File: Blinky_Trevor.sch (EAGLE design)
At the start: 15 parts, among them IC1 OP-DUALRM

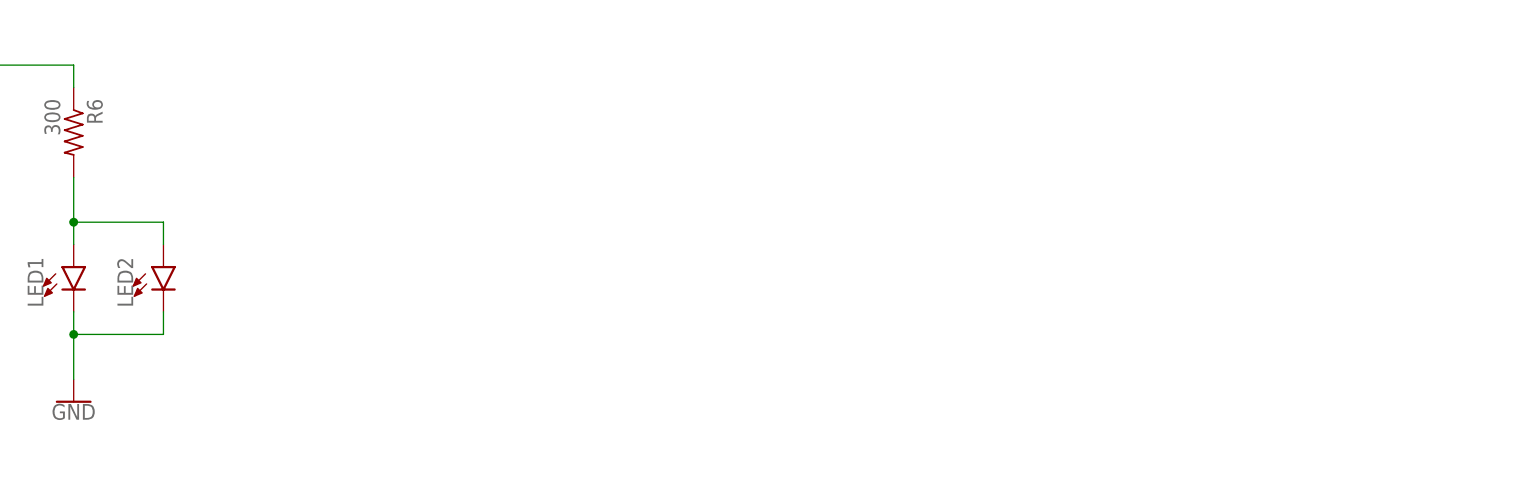
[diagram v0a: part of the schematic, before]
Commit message: Added LED Pattern
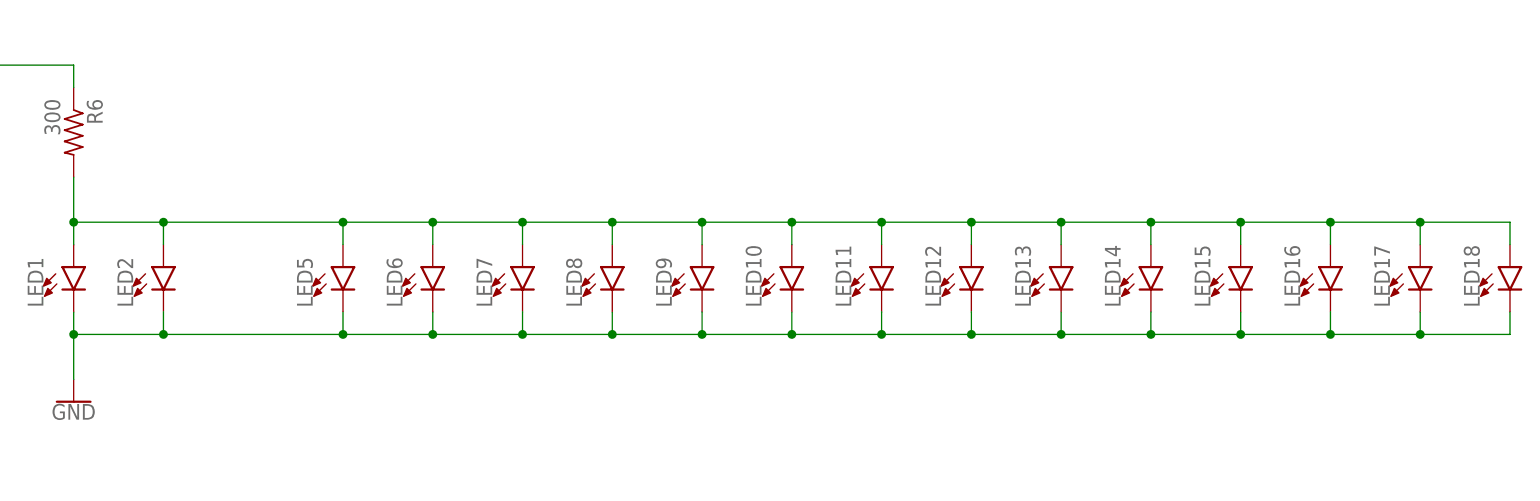
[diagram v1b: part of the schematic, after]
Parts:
- added LED10, LED11, LED12, LED13, LED14, LED15, LED16, LED17, LED18, LED5, LED6, LED7, LED8, LED9: (no value), CalvEngIO-LED:LED0603
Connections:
- net GND: now also LED10.C, LED11.C, LED12.C, LED13.C, LED14.C, LED15.C, LED16.C, LED17.C, LED18.C, LED5.C, LED6.C, LED7.C, LED8.C, LED9.C
- net N$6: now also LED10.A, LED11.A, LED12.A, LED13.A, LED14.A, LED15.A, LED16.A, LED17.A, LED18.A, LED5.A, LED6.A, LED7.A, LED8.A, LED9.A
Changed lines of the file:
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@@
 <part name="GND6" library="CalvEngIO-Symbols" deviceset="GND" device=""/>
 <part name="C2" library="CalvEngIO-Passives" deviceset="CAPACITOR" device="0402" value="100nF"/>
+<part name="LED5" library="CalvEngIO-LED" deviceset="LED" device="0603"/>
+<part name="LED6" library="CalvEngIO-LED" deviceset="LED" device="0603"/>
+<part name="LED7" library="CalvEngIO-LED" deviceset="LED" device="0603"/>
+<part name="LED8" library="CalvEngIO-LED" deviceset="LED" device="0603"/>
+<part name="LED9" library="CalvEngIO-LED" deviceset="LED" device="0603"/>
+<part name="LED10" library="CalvEngIO-LED" deviceset="LED" device="0603"/>
+<part name="LED11" library="CalvEngIO-LED" deviceset="LED" device="0603"/>
+<part name="LED12" library="CalvEngIO-LED" deviceset="LED" device="0603"/>
+<part name="LED13" library="CalvEngIO-LED" deviceset="LED" device="0603"/>
+<part name="LED14" library="CalvEngIO-LED" deviceset="LED" device="0603"/>
+<part name="LED15" library="CalvEngIO-LED" deviceset="LED" device="0603"/>
+<part name="LED16" library="CalvEngIO-LED" deviceset="LED" device="0603"/>
+<part name="LED17" library="CalvEngIO-LED" deviceset="LED" device="0603"/>
+<part name="LED18" library="CalvEngIO-LED" deviceset="LED" device="0603"/>
 </parts>
 <sheets>
@@
 <attribute name="VALUE" x="18.161" y="2.032" size="1.778" layer="96"/>
 </instance>
+<instance part="LED5" gate="G$1" x="187.96" y="25.4"/>
+<instance part="LED6" gate="G$1" x="198.12" y="25.4"/>
+<instance part="LED7" gate="G$1" x="208.28" y="25.4"/>
+<instance part="LED8" gate="G$1" x="218.44" y="25.4"/>
+<instance part="LED9" gate="G$1" x="228.6" y="25.4"/>
+<instance part="LED10" gate="G$1" x="238.76" y="25.4"/>
+<instance part="LED11" gate="G$1" x="248.92" y="25.4"/>
+<instance part="LED12" gate="G$1" x="259.08" y="25.4"/>
+<instance part="LED13" gate="G$1" x="269.24" y="25.4"/>
+<instance part="LED14" gate="G$1" x="279.4" y="25.4"/>
+<instance part="LED15" gate="G$1" x="289.56" y="25.4"/>
+<instance part="LED16" gate="G$1" x="299.72" y="25.4"/>
+<instance part="LED17" gate="G$1" x="309.88" y="25.4"/>
+<instance part="LED18" gate="G$1" x="320.04" y="25.4"/>
 </instances>
 <busses>
@@
 <wire x1="167.64" y1="17.78" x2="157.48" y2="17.78" width="0.1524" layer="91"/>
 <junction x="157.48" y="17.78"/>
+<pinref part="LED16" gate="G$1" pin="C"/>
+<wire x1="167.64" y1="17.78" x2="187.96" y2="17.78" width="0.1524" layer="91"/>
+<wire x1="187.96" y1="17.78" x2="198.12" y2="17.78" width="0.1524" layer="91"/>
+<wire x1="198.12" y1="17.78" x2="208.28" y2="17.78" width="0.1524" layer="91"/>
+<wire x1="208.28" y1="17.78" x2="218.44" y2="17.78" width="0.1524" layer="91"/>
+<wire x1="218.44" y1="17.78" x2="228.6" y2="17.78" width="0.1524" layer="91"/>
+<wire x1="228.6" y1="17.78" x2="238.76" y2="17.78" width="0.1524" layer="91"/>
+<wire x1="238.76" y1="17.78" x2="248.92" y2="17.78" width="0.1524" layer="91"/>
+<wire x1="248.92" y1="17.78" x2="259.08" y2="17.78" width="0.1524" layer="91"/>
+<wire x1="259.08" y1="17.78" x2="269.24" y2="17.78" width="0.1524" layer="91"/>
+<wire x1="269.24" y1="17.78" x2="279.4" y2="17.78" width="0.1524" layer="91"/>
+<wire x1="279.4" y1="17.78" x2="289.56" y2="17.78" width="0.1524" layer="91"/>
+<wire x1="289.56" y1="17.78" x2="299.72" y2="17.78" width="0.1524" layer="91"/>
+<wire x1="299.72" y1="17.78" x2="299.72" y2="20.32" width="0.1524" layer="91"/>
+<junction x="167.64" y="17.78"/>
+<pinref part="LED5" gate="G$1" pin="C"/>
+<wire x1="187.96" y1="20.32" x2="187.96" y2="17.78" width="0.1524" layer="91"/>
+<junction x="187.96" y="17.78"/>
+<pinref part="LED6" gate="G$1" pin="C"/>
+<wire x1="198.12" y1="20.32" x2="198.12" y2="17.78" width="0.1524" layer="91"/>
+<junction x="198.12" y="17.78"/>
+<pinref part="LED7" gate="G$1" pin="C"/>
+<wire x1="208.28" y1="20.32" x2="208.28" y2="17.78" width="0.1524" layer="91"/>
+<junction x="208.28" y="17.78"/>
+<pinref part="LED8" gate="G$1" pin="C"/>
+<wire x1="218.44" y1="20.32" x2="218.44" y2="17.78" width="0.1524" layer="91"/>
+<junction x="218.44" y="17.78"/>
+<pinref part="LED9" gate="G$1" pin="C"/>
+<wire x1="228.6" y1="20.32" x2="228.6" y2="17.78" width="0.1524" layer="91"/>
+<junction x="228.6" y="17.78"/>
+<pinref part="LED10" gate="G$1" pin="C"/>
+<wire x1="238.76" y1="20.32" x2="238.76" y2="17.78" width="0.1524" layer="91"/>
+<junction x="238.76" y="17.78"/>
+<pinref part="LED11" gate="G$1" pin="C"/>
+<wire x1="248.92" y1="20.32" x2="248.92" y2="17.78" width="0.1524" layer="91"/>
+<junction x="248.92" y="17.78"/>
+<pinref part="LED12" gate="G$1" pin="C"/>
+<wire x1="259.08" y1="20.32" x2="259.08" y2="17.78" width="0.1524" layer="91"/>
+<junction x="259.08" y="17.78"/>
+<pinref part="LED13" gate="G$1" pin="C"/>
+<wire x1="269.24" y1="20.32" x2="269.24" y2="17.78" width="0.1524" layer="91"/>
+<junction x="269.24" y="17.78"/>
+<pinref part="LED14" gate="G$1" pin="C"/>
+<wire x1="279.4" y1="20.32" x2="279.4" y2="17.78" width="0.1524" layer="91"/>
+<junction x="279.4" y="17.78"/>
+<pinref part="LED15" gate="G$1" pin="C"/>
+<wire x1="289.56" y1="20.32" x2="289.56" y2="17.78" width="0.1524" layer="91"/>
+<junction x="289.56" y="17.78"/>
+<pinref part="LED18" gate="G$1" pin="C"/>
+<wire x1="320.04" y1="20.32" x2="320.04" y2="17.78" width="0.1524" layer="91"/>
+<wire x1="320.04" y1="17.78" x2="309.88" y2="17.78" width="0.1524" layer="91"/>
+<junction x="299.72" y="17.78"/>
+<pinref part="LED17" gate="G$1" pin="C"/>
+<wire x1="309.88" y1="17.78" x2="299.72" y2="17.78" width="0.1524" layer="91"/>
+<wire x1="309.88" y1="20.32" x2="309.88" y2="17.78" width="0.1524" layer="91"/>
+<junction x="309.88" y="17.78"/>
 </segment>
 <segment>
@@
 <wire x1="167.64" y1="30.48" x2="167.64" y2="27.94" width="0.1524" layer="91"/>
 <junction x="157.48" y="30.48"/>
-</segment>
-</net>
+<pinref part="LED16" gate="G$1" pin="A"/>
+<wire x1="167.64" y1="30.48" x2="187.96" y2="30.48" width="0.1524" layer="91"/>
+<wire x1="187.96" y1="30.48" x2="198.12" y2="30.48" width="0.1524" layer="91"/>
+<wire x1="198.12" y1="30.48" x2="208.28" y2="30.48" width="0.1524" layer="91"/>
+<wire x1="208.28" y1="30.48" x2="218.44" y2="30.48" width="0.1524" layer="91"/>
+<wire x1="218.44" y1="30.48" x2="228.6" y2="30.48" width="0.1524" layer="91"/>
+<wire x1="228.6" y1="30.48" x2="238.76" y2="30.48" width="0.1524" layer="91"/>
+<wire x1="238.76" y1="30.48" x2="248.92" y2="30.48" width="0.1524" layer="91"/>
+<wire x1="248.92" y1="30.48" x2="259.08" y2="30.48" width="0.1524" layer="91"/>
+<wire x1="259.08" y1="30.48" x2="269.24" y2="30.48" width="0.1524" layer="91"/>
+<wire x1="269.24" y1="30.48" x2="279.4" y2="30.48" width="0.1524" layer="91"/>
+<wire x1="279.4" y1="30.48" x2="289.56" y2="30.48" width="0.1524" layer="91"/>
+<wire x1="289.56" y1="30.48" x2="299.72" y2="30.48" width="0.1524" layer="91"/>
+<wire x1="299.72" y1="30.48" x2="299.72" y2="27.94" width="0.1524" layer="91"/>
+<junction x="167.64" y="30.48"/>
+<pinref part="LED15" gate="G$1" pin="A"/>
+<wire x1="289.56" y1="27.94" x2="289.56" y2="30.48" width="0.1524" layer="91"/>
+<junction x="289.56" y="30.48"/>
+<pinref part="LED14" gate="G$1" pin="A"/>
+<wire x1="279.4" y1="27.94" x2="279.4" y2="30.48" width="0.1524" layer="91"/>
+<junction x="279.4" y="30.48"/>
+<pinref part="LED13" gate="G$1" pin="A"/>
+<wire x1="269.24" y1="27.94" x2="269.24" y2="30.48" width="0.1524" layer="91"/>
+<junction x="269.24" y="30.48"/>
+<pinref part="LED12" gate="G$1" pin="A"/>
+<wire x1="259.08" y1="27.94" x2="259.08" y2="30.48" width="0.1524" layer="91"/>
+<junction x="259.08" y="30.48"/>
+<pinref part="LED11" gate="G$1" pin="A"/>
+<wire x1="248.92" y1="27.94" x2="248.92" y2="30.48" width="0.1524" layer="91"/>
+<junction x="248.92" y="30.48"/>
+<pinref part="LED10" gate="G$1" pin="A"/>
+<wire x1="238.76" y1="27.94" x2="238.76" y2="30.48" width="0.1524" layer="91"/>
+<junction x="238.76" y="30.48"/>
+<pinref part="LED9" gate="G$1" pin="A"/>
+<wire x1="228.6" y1="27.94" x2="228.6" y2="30.48" width="0.1524" layer="91"/>
+<junction x="228.6" y="30.48"/>
+<pinref part="LED8" gate="G$1" pin="A"/>
+<wire x1="218.44" y1="27.94" x2="218.44" y2="30.48" width="0.1524" layer="91"/>
+<junction x="218.44" y="30.48"/>
+<pinref part="LED7" gate="G$1" pin="A"/>
+<wire x1="208.28" y1="27.94" x2="208.28" y2="30.48" width="0.1524" layer="91"/>
+<junction x="208.28" y="30.48"/>
+<pinref part="LED6" gate="G$1" pin="A"/>
+<wire x1="198.12" y1="27.94" x2="198.12" y2="30.48" width="0.1524" layer="91"/>
+<junction x="198.12" y="30.48"/>
+<pinref part="LED5" gate="G$1" pin="A"/>
+<wire x1="187.96" y1="27.94" x2="187.96" y2="30.48" width="0.1524" layer="91"/>
+<junction x="187.96" y="30.48"/>
+<pinref part="LED17" gate="G$1" pin="A"/>
+<wire x1="299.72" y1="30.48" x2="309.88" y2="30.48" width="0.1524" layer="91"/>
+<wire x1="309.88" y1="30.48" x2="309.88" y2="27.94" width="0.1524" layer="91"/>
+<junction x="299.72" y="30.48"/>
+<pinref part="LED18" gate="G$1" pin="A"/>
+<wire x1="309.88" y1="30.48" x2="320.04" y2="30.48" width="0.1524" layer="91"/>
+<wire x1="320.04" y1="30.48" x2="320.04" y2="27.94" width="0.1524" layer="91"/>
+<junction x="309.88" y="30.48"/>
+</segment>
+</net>
